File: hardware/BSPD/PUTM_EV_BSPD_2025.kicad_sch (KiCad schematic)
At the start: 38 parts, among them J1 BS1, J2 BS2, J3 BS2, J5 SDC, K2 TE AXICOM IM07DTS, Q1 BS170F, U10 LM393B, U12 74AHC1G08, U3 74HC2G14-Q100, U5 74AHC1G08, U8 NE555DR

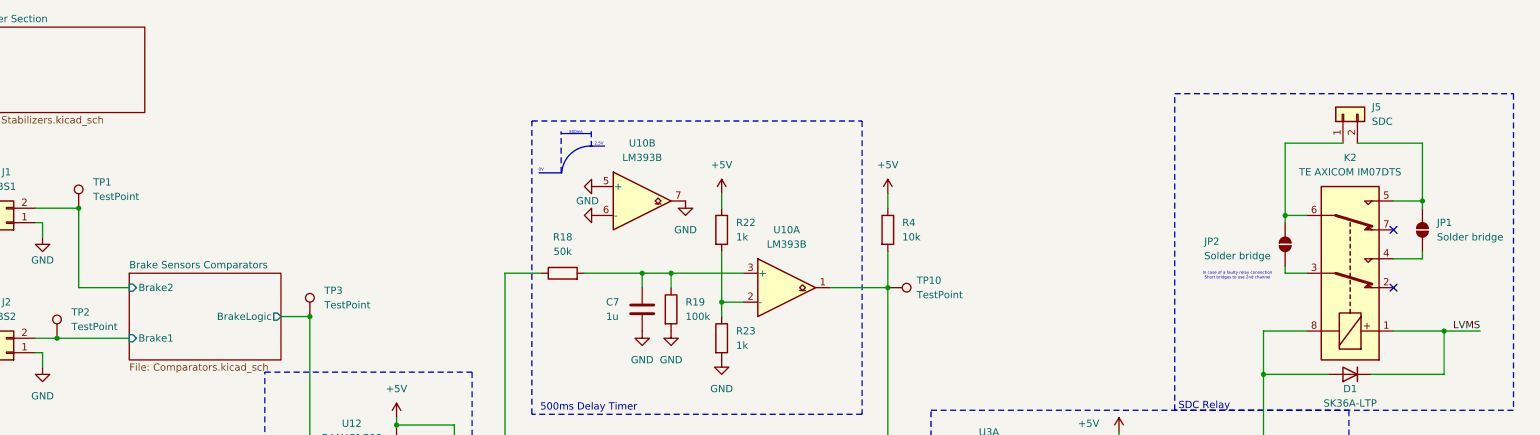
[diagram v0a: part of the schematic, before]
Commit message: Fixed relay routing + changed board shape
Board shape changed to accomodate M3 mounting holes, matching older BSPD's.
Fixed an issue where the relay coil was no connected to LVMS due to skill issues in hierarhical sheeting.
LVMS (+24VDC) line breakaway placed behind the fuse.
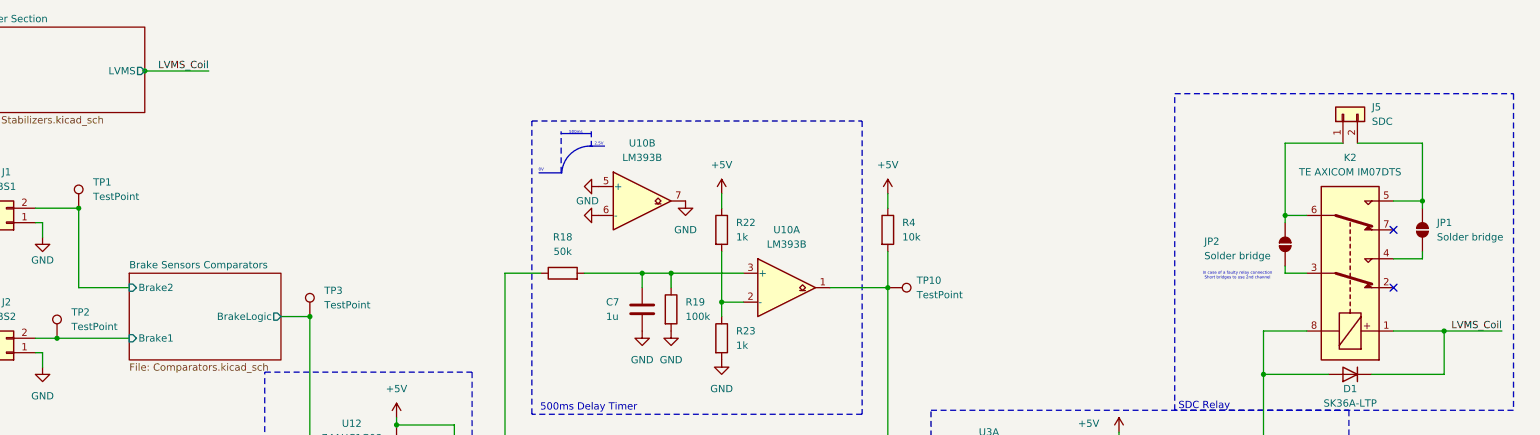
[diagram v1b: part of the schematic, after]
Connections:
- net LVMS renamed LVMS_Coil
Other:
- sheet Power Section ports: added LVMS; removed none
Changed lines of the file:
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@@
 	)
 	(junction
+		(at 43.3719 24.13)
+		(diameter 0)
+		(color 0 0 0 0)
+	)
+	(junction
 		(at 231.14 99.06)
 		(diameter 0)
@@
 		)
 	)
+	(wire
+		(pts
+			(xy 271.78 69.85) (xy 281.94 69.85)
+		)
+		(stroke
+			(width 0)
+			(type default)
+		)
+	)
 	(polyline
 		(pts
@@
 	(wire
 		(pts
+			(xy 43.18 24.13) (xy 43.3719 24.13)
+		)
+		(stroke
+			(width 0)
+			(type default)
+		)
+	)
+	(wire
+		(pts
 			(xy 267.97 46.99) (xy 267.97 48.26)
 		)
@@
 		)
 	)
-	(wire
-		(pts
-			(xy 278.13 69.85) (xy 271.78 69.85)
-		)
-		(stroke
-			(width 0)
-			(type default)
-		)
-	)
 	(polyline
 		(pts
@@
 	(wire
 		(pts
+			(xy 43.3719 24.13) (xy 54.61 24.13)
+		)
+		(stroke
+			(width 0)
+			(type default)
+		)
+	)
+	(wire
+		(pts
 			(xy 97.79 102.87) (xy 97.79 106.68)
 		)
@@
 		)
 	)
-	(label "LVMS"
-		(at 278.13 69.85 180)
+	(label "LVMS_Coil"
+		(at 54.61 24.13 180)
+		(effects
+			(font
+				(size 1.27 1.27)
+			)
+			(justify right bottom)
+		)
+	)
+	(label "LVMS_Coil"
+		(at 281.94 69.85 180)
 		(effects
 			(font
@@
 			)
 		)
+		(pin "LVMS" output
+			(at 43.3719 24.13 0)
+			(effects
+				(font
+					(size 1.27 1.27)
+				)
+				(justify right)
+			)
+		)

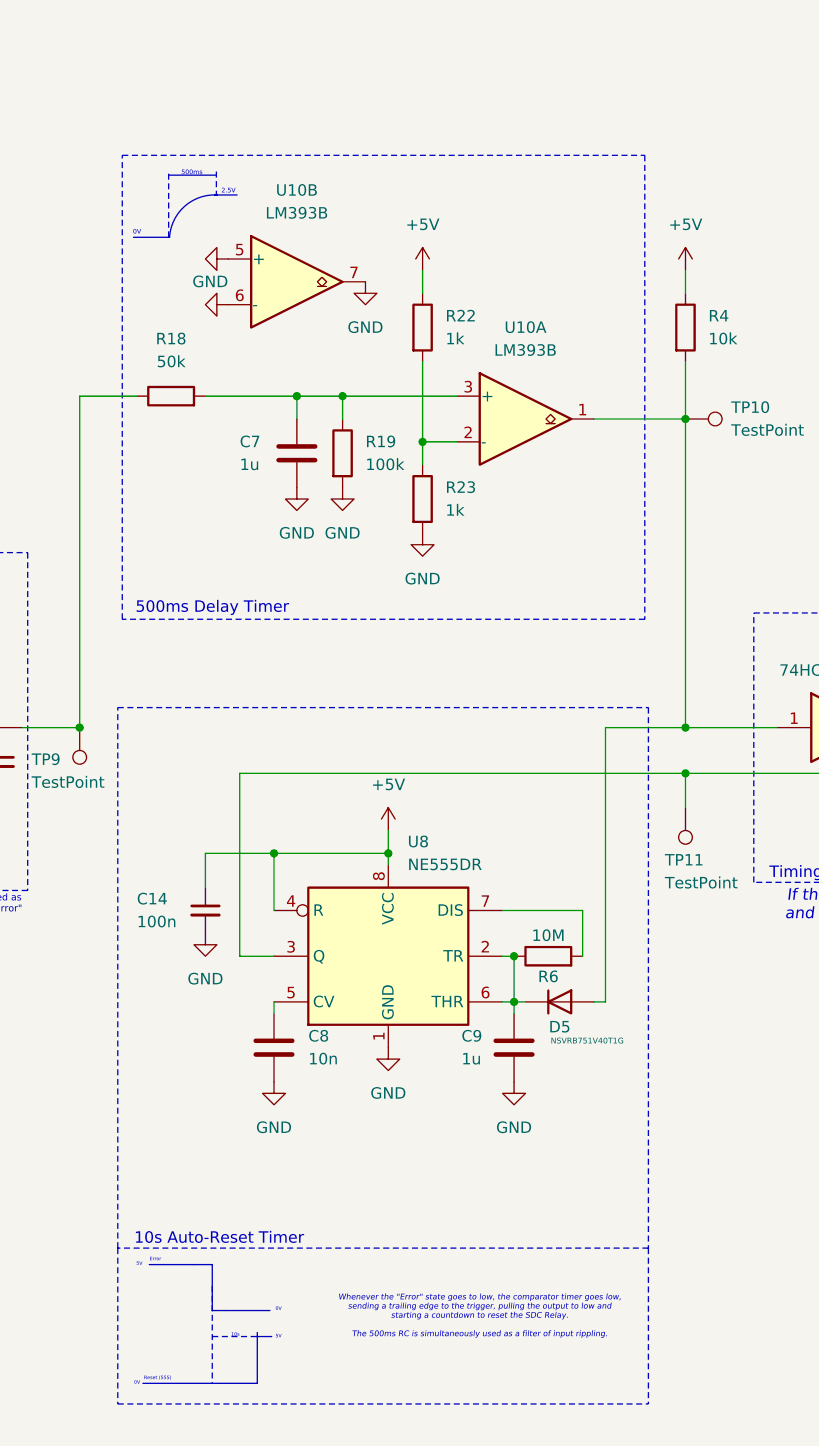
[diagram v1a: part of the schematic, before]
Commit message: Minor changes. Read ext. description for info.
Removed isolated copper (ground) islands on both layers
Changed timing capacitors values to compensate DC Bias (+0.5uF)
Changed board shape 
Relocated TVS Diodes to be directly connected with inputs
Fixed relay wiring issues
Added space for additional capacitors to compensate DC Bias if needed
Fixed overlapped part references
Added mounting holes, and relocated a connector to accomodate screw head.
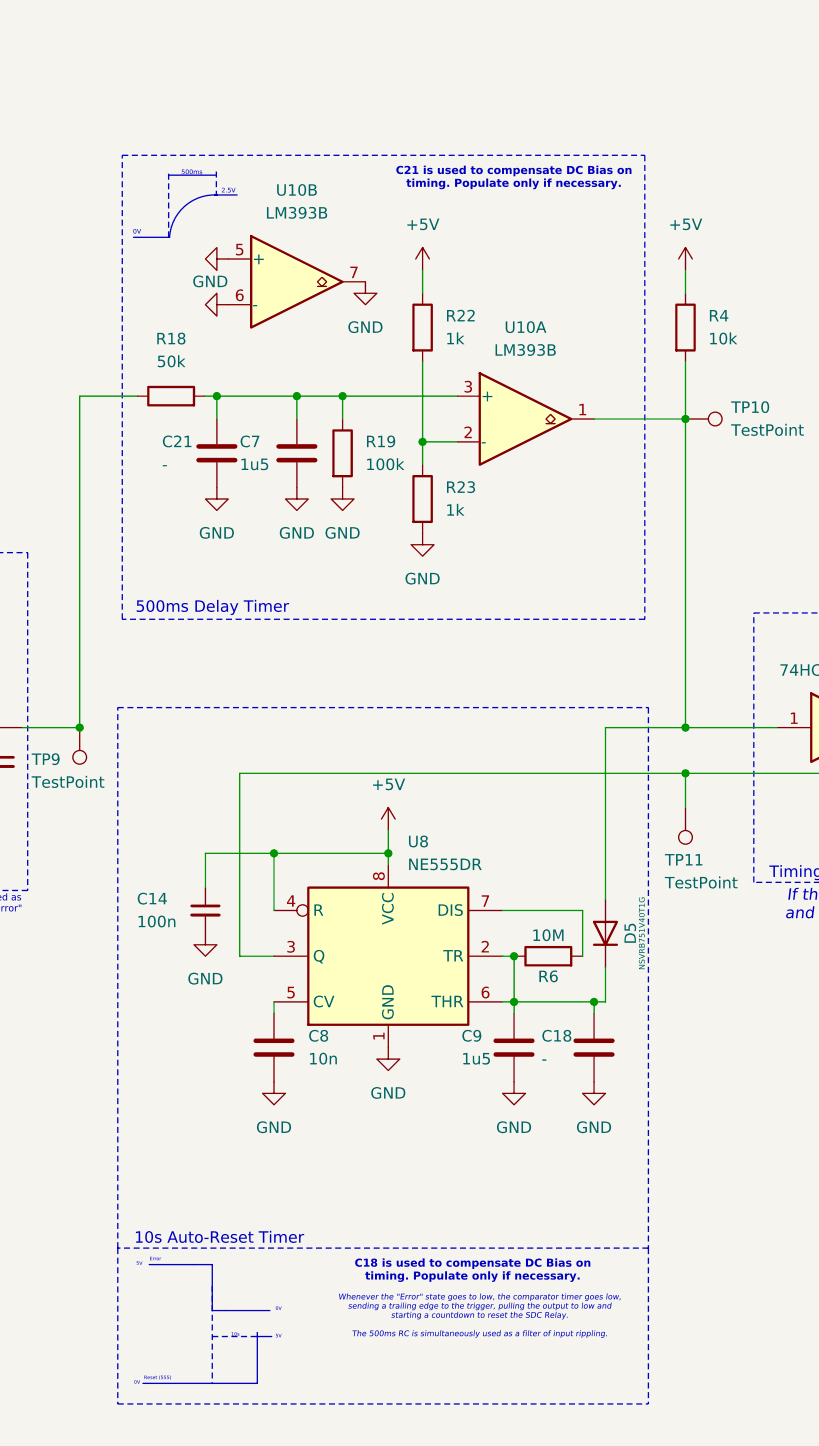
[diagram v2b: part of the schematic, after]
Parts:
- added C18, C21: -, Capacitor_SMD:C_0603_1608Metric, symbol Device:C
- C7, C9: value 1u -> 1u5
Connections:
- net GND: now also C18.2, C21.1
- net at C7.1, R18.2, R19.1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: now also C21.2
- net at C9.1, D5.1 (K), R6.1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: now also C18.1
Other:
- note added: "C18 is used to compensate DC Bias on timing. Populate only if necessary."
- note added: "C21 is used to compensate DC Bias on timing. Populate only if necessary."
- moved on the sheet: D5

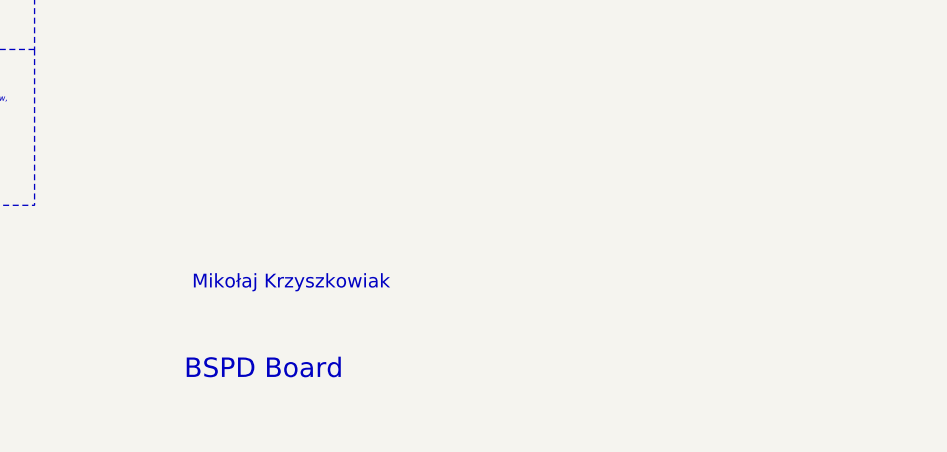
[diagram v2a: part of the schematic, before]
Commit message: Added silkscreen descriptions
Added descriptions of potentiometers (RV1-RV3) to ease up threshold regulation.
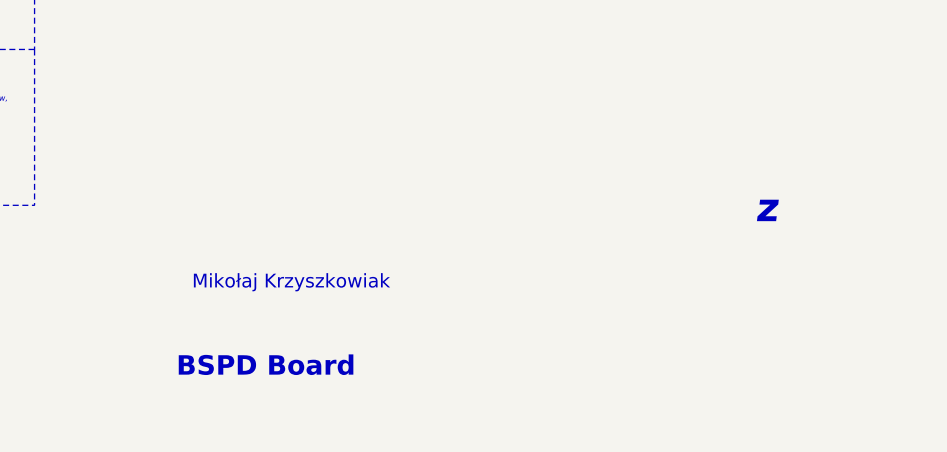
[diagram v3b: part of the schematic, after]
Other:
- note added: "z"
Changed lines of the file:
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@@
 	(text "BSPD Board"
 		(exclude_from_sim no)
-		(at 195.326 189.992 0)
+		(at 195.58 189.738 0)
 		(effects
 			(font
 				(size 2.159 2.159)
+				(thickness 0.4318)
+				(bold yes)
 				(color 132 0 0 1)
 			)
@@
 			)
 		)
+	)
+	(text "z"
+		(exclude_from_sim no)
+		(at 251.206 172.212 0)
+		(effects
+			(font
+				(size 3.175 3.175)
+				(thickness 0.7874)
+				(bold yes)
+				(italic yes)
+				(color 132 0 0 0)
+			)
+		)

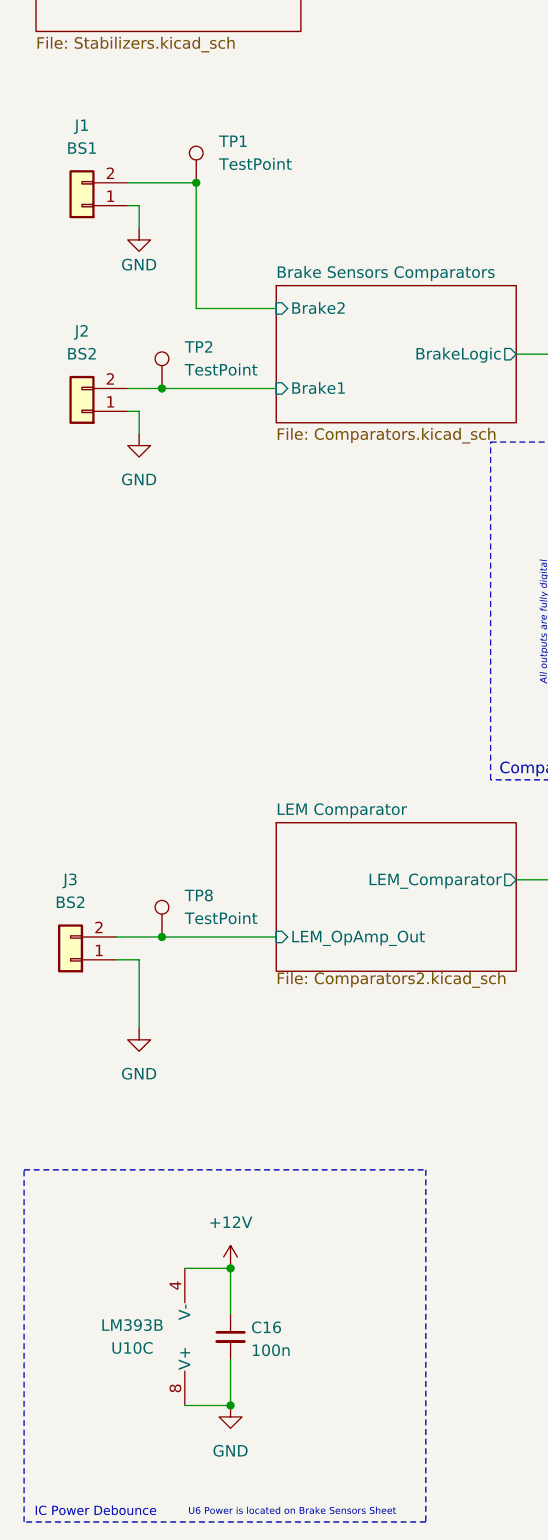
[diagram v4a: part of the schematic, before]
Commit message: Changes for 2026 Rules - added pull down resistors and reversed polarity of comparator (nie pozdrawiam Zdrajcy)
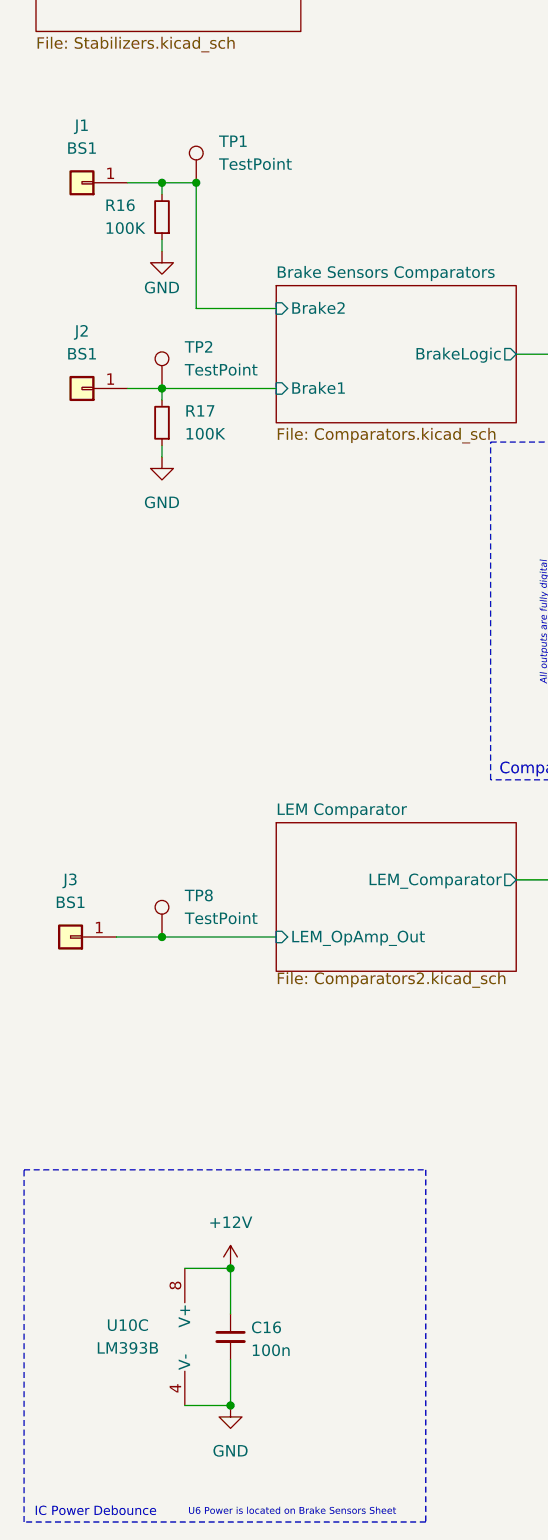
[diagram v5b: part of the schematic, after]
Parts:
- removed J2, J3: BS2, footprints:Wire_StrainRelief, symbol Connector_Generic:Conn_01x02
- added J2, J3: BS1, Connector_Wire:SolderWire-0.1sqmm_1x01_D0.4mm_OD1mm_Relief, symbol Connector_Generic:Conn_01x01
- added R16, R17: 100K, Resistor_SMD:R_0603_1608Metric_Pad0.98x0.95mm_HandSolder, symbol Device:R_Small
- J1: footprint footprints:Wire_StrainRelief -> Connector_Wire:SolderWire-0.1sqmm_1x01_D0.4mm_OD1mm_Relief; symbol Connector_Generic:Conn_01x02 -> Connector_Generic:Conn_01x01
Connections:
- net +12V: now also U10.8 (V+); no longer U10.4 (V-)
- net Brake Sensors Comparators/Brake1: now also J2.1 (Pin_1), R17.2
- net Brake Sensors Comparators/Brake2: now also J1.1 (Pin_1), R16.2; no longer J1.2 (Pin_2)
- net GND: now also U10.4 (V-), R16.1, R17.1; no longer J1.1 (Pin_1), U10.8 (V+)
- net LEM Comparator/LEM_OpAmp_Out: now also J3.1 (Pin_1)
